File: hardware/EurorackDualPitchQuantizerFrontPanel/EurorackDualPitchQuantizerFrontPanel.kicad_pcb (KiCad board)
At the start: 2 copper layers, 50.8 x 136.2 mm, 4 parts

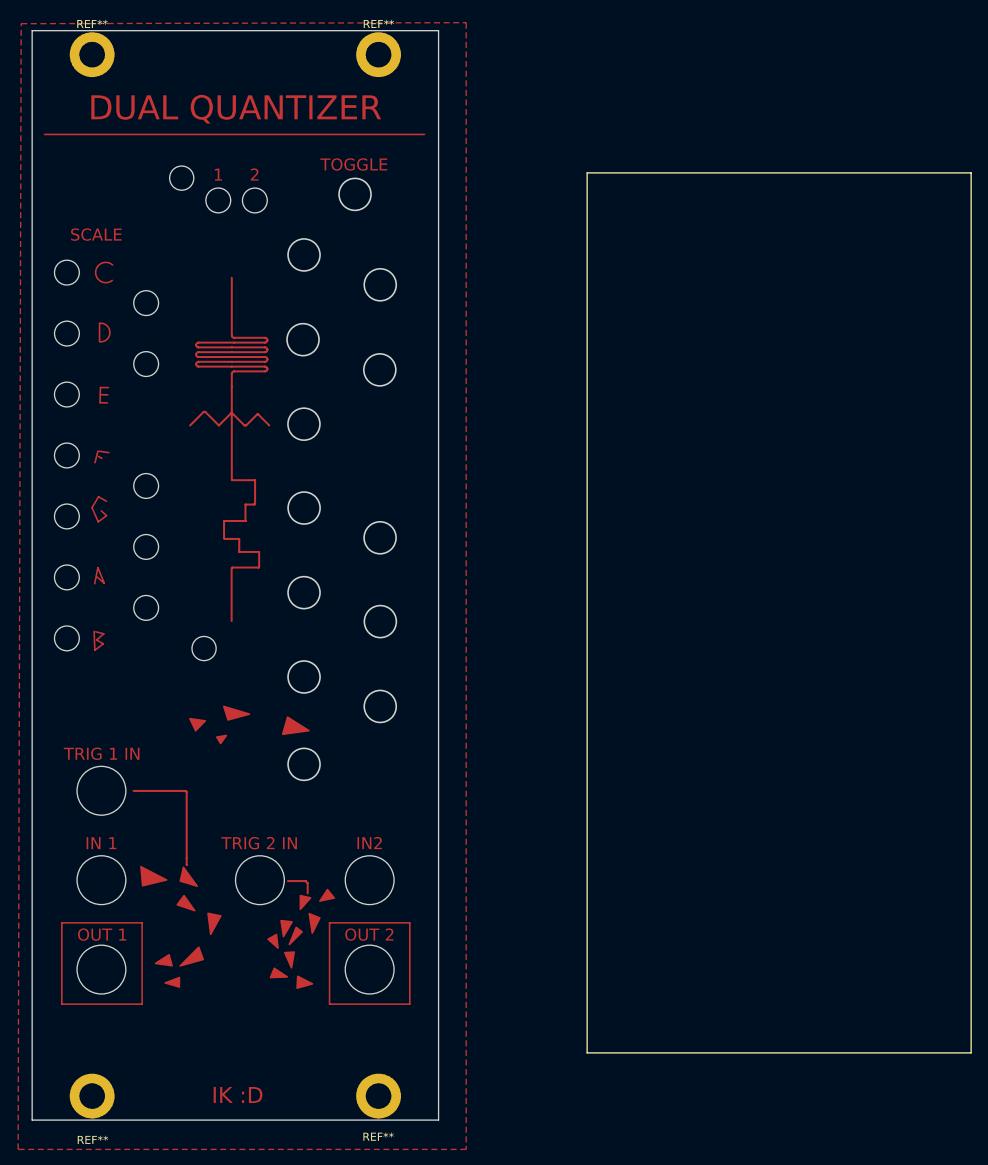
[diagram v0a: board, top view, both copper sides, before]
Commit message: Got Rev 1.2 complete. It should be manufacturable and fit into eurorack standards.
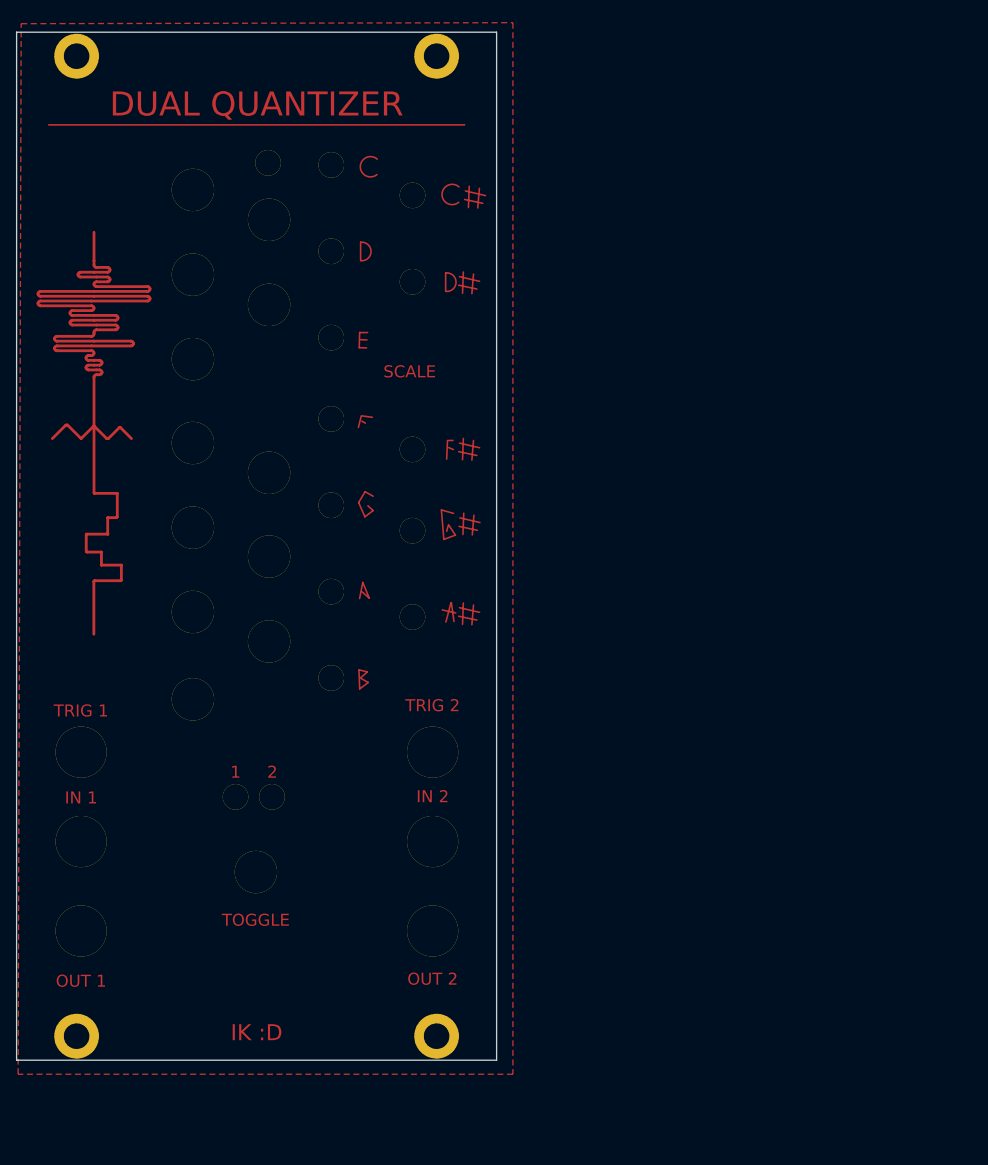
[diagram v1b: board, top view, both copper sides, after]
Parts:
- added REF**: MountingHole_3.2mm_M3, MountingHole:MountingHole_3.2mm_M3, F.Cu at (61.5, 25.4)
- added REF**: MountingHole_6.4mm_M6, MountingHole:MountingHole_6.4mm_M6, B.Cu at (20.1, 95.0)
- added REF**: MountingHole_5.3mm_M5, MountingHole:MountingHole_5.3mm_M5, B.Cu at (34.0, 56.4)
- added REF**: MountingHole_3.2mm_M3, MountingHole:MountingHole_3.2mm_M3, B.Cu at (61.5, 67.3)
- added REF**: MountingHole_5.3mm_M5, MountingHole:MountingHole_5.3mm_M5, B.Cu at (34.0, 35.3)
- added REF**: MountingHole_3.2mm_M3, MountingHole:MountingHole_3.2mm_M3, B.Cu at (51.3, 53.3)
- added REF**: MountingHole_3.2mm_M3, MountingHole:MountingHole_3.2mm_M3, B.Cu at (51.3, 32.4)
- added REF**: MountingHole_5.3mm_M5, MountingHole:MountingHole_5.3mm_M5, B.Cu at (43.6, 60.1)
- added REF**: MountingHole_3.2mm_M3, MountingHole:MountingHole_3.2mm_M3, B.Cu at (61.5, 36.2)
- added REF**: MountingHole_3.2mm_M3, MountingHole:MountingHole_3.2mm_M3, B.Cu at (43.4, 21.3)
- added REF**: MountingHole_5.3mm_M5, MountingHole:MountingHole_5.3mm_M5, B.Cu at (34.0, 77.5)
- added REF**: MountingHole_3.2mm_M3, MountingHole:MountingHole_3.2mm_M3, F.Cu at (51.3, 21.6)
- added REF**: MountingHole_6.4mm_M6, MountingHole:MountingHole_6.4mm_M6, B.Cu at (64.0, 117.3)
- added REF**: MountingHole_3.2mm_M3, MountingHole:MountingHole_3.2mm_M3, B.Cu at (39.4, 100.6)
- added REF**: MountingHole_3.2mm_M3, MountingHole:MountingHole_3.2mm_M3, B.Cu at (51.3, 85.7)
- added REF**: MountingHole_6.4mm_M6, MountingHole:MountingHole_6.4mm_M6, B.Cu at (64.0, 106.2)
- added REF**: MountingHole_3.2mm_M3, MountingHole:MountingHole_3.2mm_M3, B.Cu at (43.9, 100.6)
- added REF**: MountingHole_5.3mm_M5, MountingHole:MountingHole_5.3mm_M5, B.Cu at (34.0, 45.9)
- added REF**: MountingHole_3.2mm_M3, MountingHole:MountingHole_3.2mm_M3, B.Cu at (51.3, 43.2)
- added REF**: MountingHole_5.3mm_M5, MountingHole:MountingHole_5.3mm_M5, B.Cu at (34.0, 88.4)
- added REF**: MountingHole_5.3mm_M5, MountingHole:MountingHole_5.3mm_M5, B.Cu at (34.0, 66.9)
- added REF**: MountingHole_5.3mm_M5, MountingHole:MountingHole_5.3mm_M5, B.Cu at (41.9, 110.0)
- added REF**: MountingHole_5.3mm_M5, MountingHole:MountingHole_5.3mm_M5, B.Cu at (43.6, 81.2)
- added REF**: MountingHole_6.4mm_M6, MountingHole:MountingHole_6.4mm_M6, B.Cu at (64.0, 95.0)
- added REF**: MountingHole_6.4mm_M6, MountingHole:MountingHole_6.4mm_M6, B.Cu at (20.1, 106.2)
- added REF**: MountingHole_5.3mm_M5, MountingHole:MountingHole_5.3mm_M5, B.Cu at (34.0, 24.7)
- added REF**: MountingHole_5.3mm_M5, MountingHole:MountingHole_5.3mm_M5, B.Cu at (43.6, 70.5)
- added REF**: MountingHole_6.4mm_M6, MountingHole:MountingHole_6.4mm_M6, B.Cu at (20.1, 117.3)
- added REF**: MountingHole_3.2mm_M3, MountingHole:MountingHole_3.2mm_M3, B.Cu at (61.5, 78.1)
- added REF**: MountingHole_5.3mm_M5, MountingHole:MountingHole_5.3mm_M5, B.Cu at (43.6, 39.1)
- added REF**: MountingHole_3.2mm_M3, MountingHole:MountingHole_3.2mm_M3, B.Cu at (61.5, 57.1)
- added REF**: MountingHole_5.3mm_M5, MountingHole:MountingHole_5.3mm_M5, B.Cu at (43.6, 28.4)
- added REFde: MountingHole_3.2mm_M3, MountingHole:MountingHole_3.2mm_M3, B.Cu at (51.3, 74.9)
- added REFe: MountingHole_3.2mm_M3, MountingHole:MountingHole_3.2mm_M3, B.Cu at (51.3, 64.1)
- REF** (x4): moved to B.Cu
- moved REF** 10.4 mm to (64.5, 130.5), turned to 180 degrees
- moved REF** 7.73 mm to (19.5, 130.5), turned to 180 degrees
- moved REF** 7.26 mm to (64.5, 8.00), turned to 180 degrees
- moved REF** 1.96 mm to (19.5, 8.00), turned to 180 degrees
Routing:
- net (no net): track 151.0 -> 201.6 mm
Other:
- board size 50.8 x 136.2 mm -> 60 x 128.5 mm
- board text added: "IN 2"
- board text added: "Ilmari Hirvonen DPQ Front Rev 1.2 2022-12-11 CERN-OHL-S v2"
- board text added: "TRIG 1"
- board text added: "TRIG 2"
- board text removed: "IN2"
- board text removed: "TRIG 1 IN"
- board text removed: "TRIG 2 IN"
